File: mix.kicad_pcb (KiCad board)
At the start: 2 copper layers, 152.1 x 64.7 mm, 65 parts, among them J1 Conn_02x05_Odd_Even, J2 AudioJack2_SwitchT, J3 AudioJack2_SwitchT, J4 AudioJack2_SwitchT, J5 AudioJack2_SwitchT, J6 AudioJack2, Q1 BCM847, Q2 BCM847, U1 TL074, U2 TL072

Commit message: v0
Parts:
- moved D4 8.58 mm to (170.3, 47.5)
- moved R21 8.58 mm to (167.6, 47.0)
- moved D3 8.58 mm to (177.9, 47.5)
- moved D5 8.58 mm to (162.7, 47.5)
- moved D6 8.58 mm to (155.1, 47.5)
- moved H13 8.58 mm to (179.2, 81.1)
- moved H14 8.58 mm to (171.6, 81.1)
- moved H15 8.58 mm to (164.0, 81.1)
- moved H16 8.58 mm to (156.3, 81.1)
- moved R20 8.58 mm to (175.3, 47.0)
- moved R22 8.58 mm to (160.0, 47.0)
- moved R23 8.58 mm to (152.4, 47.0)
- moved R16 7.88 mm to (175.3, 51.4), turned to 0 degrees
- moved H17 7.17 mm to (194.4, 90.7)
- moved J6 7.17 mm to (194.4, 57.1)
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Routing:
- net GND: track 28.7 -> 63.0 mm
- net Net-(Q2A-B1): track 3.03 -> 16.3 mm
- net /OUT: track 42.5 -> 32.2 mm
- net +12V: track 157.8 -> 148.2 mm
- net Net-(D3-K): track 9.42 -> 16.8 mm
- net Net-(R18-Pad1): track 15.4 -> 9.11 mm
- net Net-(R17-Pad1): track 15.4 -> 10.7 mm
- net Net-(D6-K): track 4.67 -> 8.47 mm
- net Net-(U1B--): track 18.0 -> 15.0 mm
- net Net-(D5-K): track 9.06 -> 11.9 mm
- net /OUT': track 58.7 -> 56.2 mm, vias 2 -> 0
- net Net-(D4-K): track 7.53 -> 9.74 mm
- net -12V: track 107.6 -> 106.0 mm
- net Net-(R6-Pad1): track 6.78 -> 8.20 mm
- net Net-(Q1B-B2): track 2.42 -> 3.65 mm
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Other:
- outline, holes or cut-outs redrawn
- board text added: "S"
- board text added: "T"

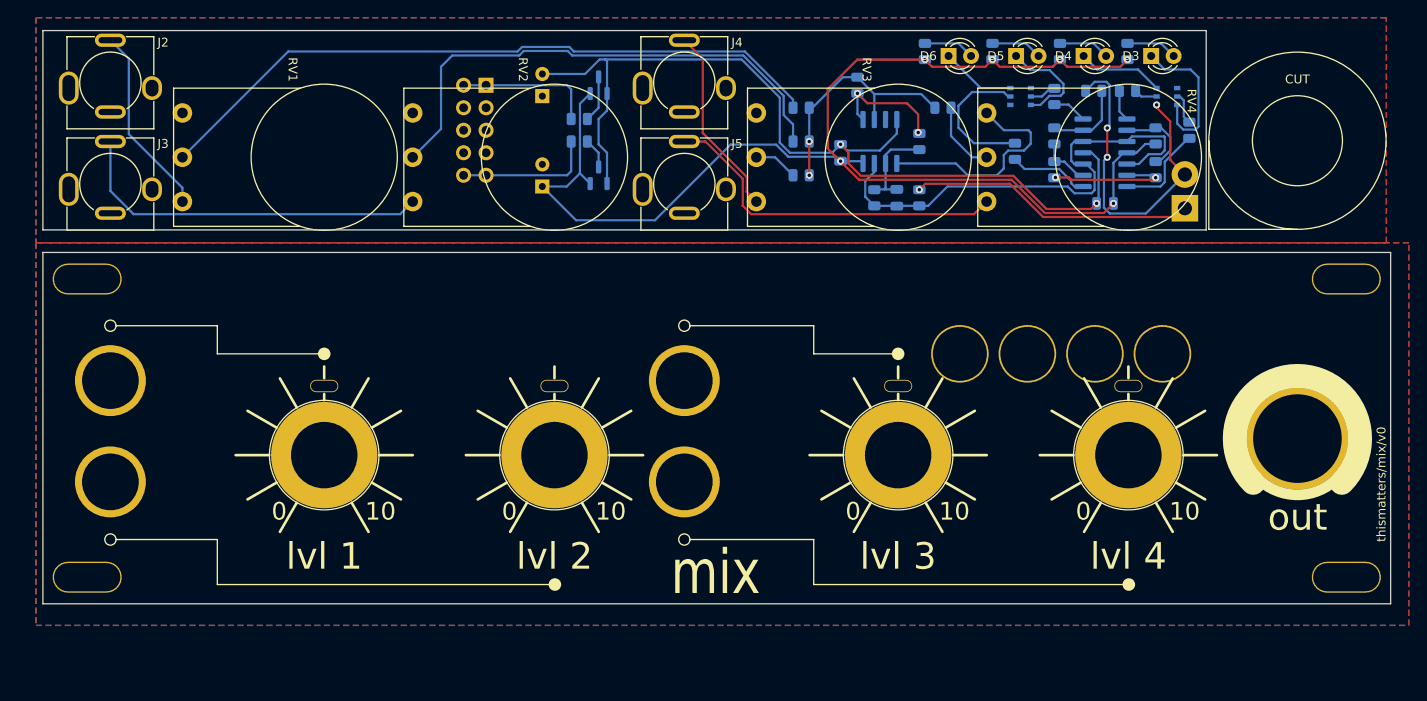
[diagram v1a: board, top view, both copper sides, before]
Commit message: adding pcb to readme
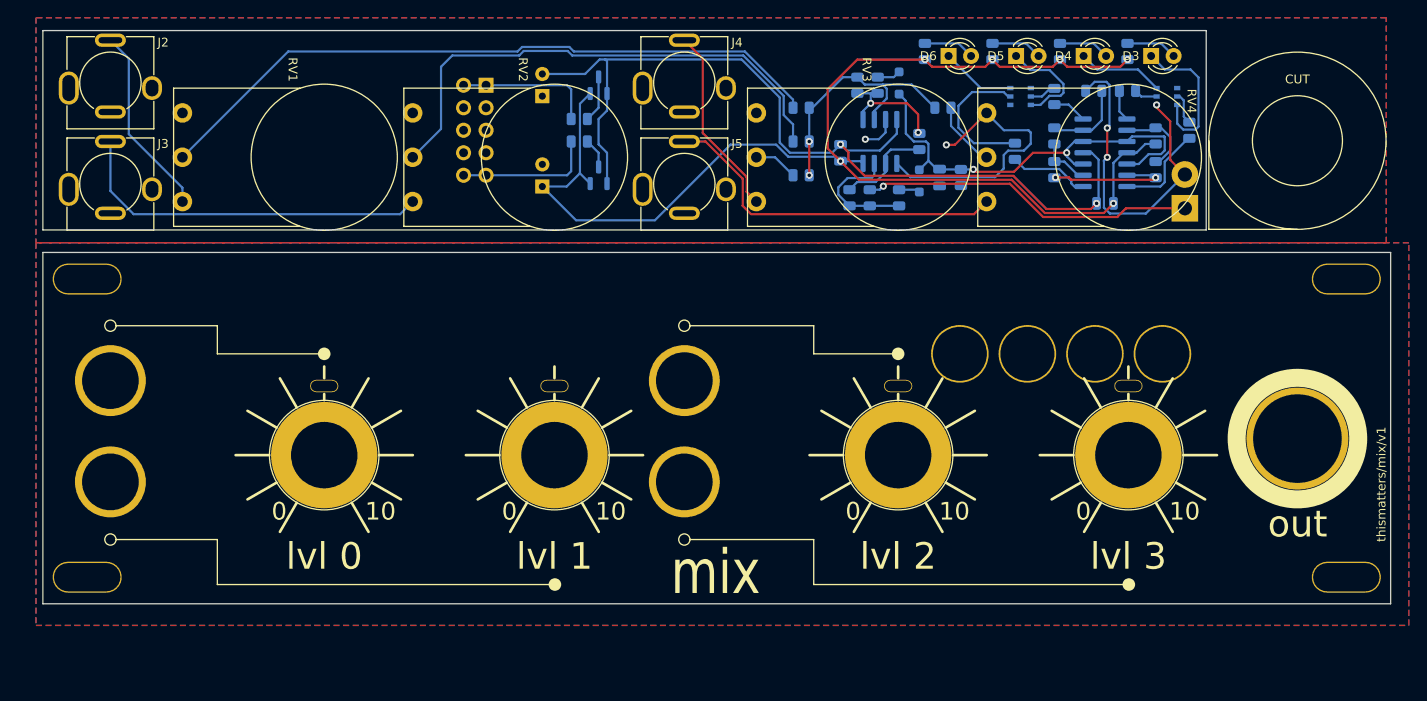
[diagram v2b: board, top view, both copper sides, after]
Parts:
- added D7: 1N4148, Diode_SMD:D_SOD-323_HandSoldering, B.Cu at (149.5, 50.5)
- added D8: 1N4148, Diode_SMD:D_SOD-323_HandSoldering, B.Cu at (151.8, 61.6)
- added R24: 100K, Resistor_SMD:R_0805_2012Metric, B.Cu at (156.5, 61.2)
- added R25: 10K, Resistor_SMD:R_0805_2012Metric, B.Cu at (147.1, 50.8)
- added R26: 10K, Resistor_SMD:R_0805_2012Metric, B.Cu at (149.5, 63.5)
- C5: value 15p -> 100n
- H10: value lvl 2 -> lvl 1
- H11: value lvl 3 -> lvl 2
- H12: value lvl 4 -> lvl 3
- H5, H6, H7, H8: footprint Eurorack:Mech-AudioJack-Hole -> Eurorack:Mech-AudioJack-Hole-Input
- H9: value lvl 1 -> lvl 0
- moved R10 5.59 mm to (146.2, 63.5)
- moved C5 5.34 mm to (154.1, 61.2), turned to -90 degrees
- moved R9 2.79 mm to (143.9, 63.5)
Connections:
- C5 pad 2: Net-(U2B--) -> GND
- R10 pad 1: /OUT' -> Net-(R10-Pad1)
- R9 pad 2: /OUT' -> Net-(R10-Pad1)
- U2 pad 7: /OUT' -> Net-(R10-Pad1)
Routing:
- net Net-(R10-Pad1): track 0.00 -> 14.2 mm
- net GND: track 63.0 -> 73.3 mm, vias 3 -> 5
- net /OUT': track 56.2 -> 49.3 mm, vias 0 -> 2
- net /OUT: track 32.2 -> 37.8 mm
- net Net-(D7-A): track 0.00 -> 2.66 mm
- net Net-(D8-A): track 0.00 -> 2.03 mm
- net Net-(U2A--): track 27.2 -> 29.0 mm
- net Net-(R6-Pad1): track 8.20 -> 7.05 mm
- net Net-(U1A--): track 9.13 -> 8.32 mm
- net -12V: track 106.0 -> 105.4 mm
- net Net-(U1C--): track 5.87 -> 5.29 mm
- net Net-(U1B--): track 15.0 -> 14.5 mm
- net +12V: track 148.2 -> 147.7 mm
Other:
- board text added: "thismatters/mix/v1"
- board text removed: "thismatters/mix/v0"
